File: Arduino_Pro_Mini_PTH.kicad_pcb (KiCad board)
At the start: 2 copper layers, 0 parts

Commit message: Routed.
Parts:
- added C1: 10u, mfk-CRP_5.0_2.0_0.5, F.Cu at (193.7, 185.4)
- added C2: 10u, mfk-CRP_5.0_2.0_0.5, F.Cu at (196.2, 175.9)
- added C3: 100n, mfk-C_4.0_2.5_2.5_0.5, F.Cu at (189.2, 178.4)
- added C4: 100n, mfk-C_4.0_2.5_2.5_0.5, F.Cu at (177.2, 183.5)
- added C7: 100n, mfk-C_4.0_2.5_2.5_0.5, F.Cu at (193.0, 200.7)
- added C8: 100n, mfk-C_4.0_2.5_2.5_0.5, F.Cu at (177.8, 198.1)
- added D1: LED, LED-3MM, F.Cu at (185.4, 178.4)
- added D2: LED, LED-3MM, F.Cu at (193.0, 208.9)
- added IC1: ATMEGA328P-PU, mfk-DIP-28_300_rnd, F.Cu at (185.4, 199.4)
- added P1: I/O lo, mfk-SIL-12, F.Cu at (172.7, 199.4)
- added P2: FTDI Basic, mfk-SIL-6, F.Cu at (185.4, 172.7)
- added P3: A4 A5, mfk-SIL-2, F.Cu at (194.9, 196.2)
- added P4: I/O hi, mfk-SIL-12, F.Cu at (198.1, 199.4)
- added R1: 10K, mfk-R_0.25W_RN55_vert, F.Cu at (181.6, 178.4)
- added R2: 10K, mfk-R_0.25W_RN55_vert, F.Cu at (177.2, 188.0)
- added R3: 330, mfk-R_0.25W_RN55_vert, F.Cu at (193.0, 205.7)
- added R4: opt, mfk-R_0.25W_RN55_vert, F.Cu at (194.3, 191.1)
- added R5: opt, mfk-R_0.25W_RN55_vert, F.Cu at (191.8, 192.4)
- added SW1: Reset, mfk-SW_PUSH_6MM, F.Cu at (175.9, 178.4)
- added U1: L4931CZ50-AP, mfk-TO-92_f321, F.Cu at (192.4, 179.7)
- added X1: CSTLS16M0X53-B0, mfk-Murata-CSTLS_X, F.Cu at (177.8, 204.5)
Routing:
- net GND: track 0.00 -> 105.2 mm
- net VCC: track 0.00 -> 74.4 mm
- net RESET: track 0.00 -> 44.0 mm
- net RXI: track 0.00 -> 34.0 mm, vias 0 -> 1
- net TXO: track 0.00 -> 32.6 mm
- net DTR: track 0.00 -> 21.4 mm
- net D9: track 0.00 -> 17.6 mm
- net A2: track 0.00 -> 14.9 mm
- net A4: track 0.00 -> 14.4 mm
- net A5: track 0.00 -> 14.4 mm
- net A3: track 0.00 -> 14.2 mm
- net A1: track 0.00 -> 12.9 mm
- net A0: track 0.00 -> 12.2 mm
- net D4: track 0.00 -> 11.2 mm
- net D8: track 0.00 -> 11.0 mm
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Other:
- board outline added: 27.9 x 45.7 mm
- board text added: "3"

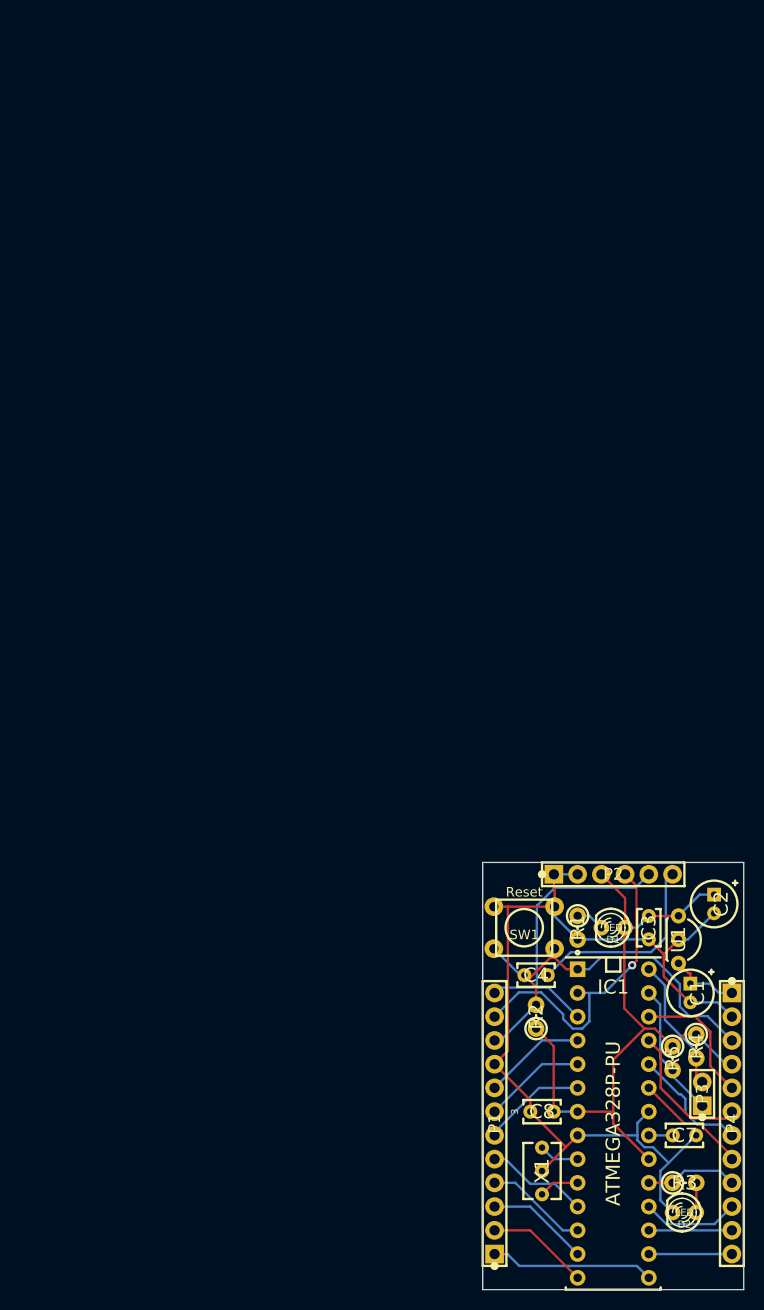
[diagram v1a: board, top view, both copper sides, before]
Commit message: Routed. Flooded. Silkscreen.
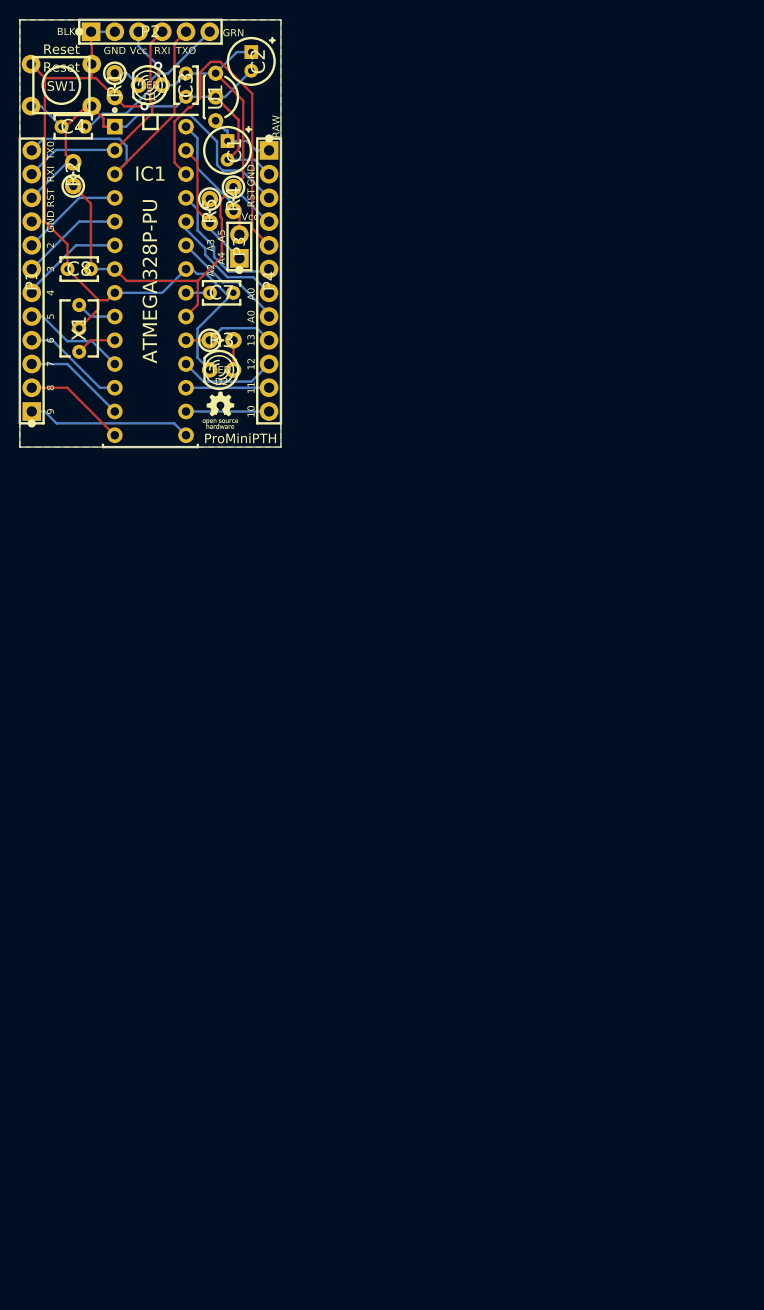
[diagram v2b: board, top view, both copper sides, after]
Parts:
- added VAL: REF, oshw-logo-150mil-FSilk, F.Cu at (143.4, 123.1)
- moved C4 103.4 mm to (127.6, 92.7)
- moved P3 103.3 mm to (145.4, 105.5)
- moved R4 103.3 mm to (144.8, 100.5)
- moved R5 103.3 mm to (142.2, 101.7)
- moved C2 102.9 mm to (146.7, 85.7)
- moved R3 102.9 mm to (143.5, 115.6)
- moved U1 102.9 mm to (142.9, 89.5)
- moved C3 102.9 mm to (139.7, 88.3)
- moved C7 102.9 mm to (143.5, 110.5)
- moved C8 102.9 mm to (128.3, 108.0)
- moved D1 102.9 mm to (135.9, 88.3)
- moved P2 102.9 mm to (135.9, 82.5)
- moved R1 102.9 mm to (132.1, 88.3)
- moved R2 102.9 mm to (127.6, 97.8)
- moved SW1 102.9 mm to (126.4, 88.3)
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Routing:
- net A3: track 14.2 -> 37.1 mm
- net RXI: track 34.0 -> 24.9 mm, vias 1 -> 0
- net DTR: track 21.4 -> 18.1 mm
- net VCC: track 74.4 -> 75.8 mm, vias 0 -> 1
- net GND: track 105.2 -> 106.3 mm, vias 0 -> 1
- net A2: track 14.9 -> 14.2 mm
- net RESET: track 44.0 -> 44.5 mm
- net A4: track 14.4 -> 13.9 mm
- net A5: track 14.4 -> 13.9 mm
- added copper zone on B.Cu, net GND
- added copper zone on F.Cu, net GND
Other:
- board text added: "10"
- board text added: "11"
- board text added: "12"
- board text added: "13"
- board text added: "2"
- board text added: "4"
- board text added: "5"
- board text added: "6"
- board text added: "7"
- board text added: "8"
- board text added: "9"
- board text added: "A0"
- board text added: "A2"
- board text added: "A3"
- board text added: "A4"
- board text added: "A5"
- board text added: "BLK"
- board text added: "GND"
- board text added: "GRN"
- board text added: "ProMiniPTH"
- board text added: "RAW"
- board text added: "RST"
- board text added: "RXI"
- board text added: "Reset"
- board text added: "TX0"
- board text added: "TXO"
- board text added: "Vcc"

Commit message: Fixed mislabeled A1. Moves OSH logo.
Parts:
- moved VAL 15.2 mm to (128.3, 124.6)
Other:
- board text added: "A1"
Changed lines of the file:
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@@
   )
   (module oshw-logo-150mil-FSilk (layer F.Cu)
-    (at 143.383 123.063)
+    (at 128.27 124.587)
     (fp_text reference VAL (at 0 0) (layer F.SilkS) hide
       (effects (font (size 0.381 0.381) (thickness 0.127)))
@@
     (effects (font (size 0.762 0.762) (thickness 0.1524)))
   )
-  (gr_text A0 (at 146.685 110.617 90) (layer F.SilkS)
-    (effects (font (size 0.762 0.762) (thickness 0.1524)))
-  )
+  (gr_text A1 (at 146.685 110.617 90) (layer F.SilkS)
+    (effects (font (size 0.762 0.762) (thickness 0.1524)))
+  )
